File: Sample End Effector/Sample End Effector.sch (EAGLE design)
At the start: 24 parts, among them IC1 LM2936MP-3.0, IC2 LM2936MP-3.0, U2 XBEE-1B3

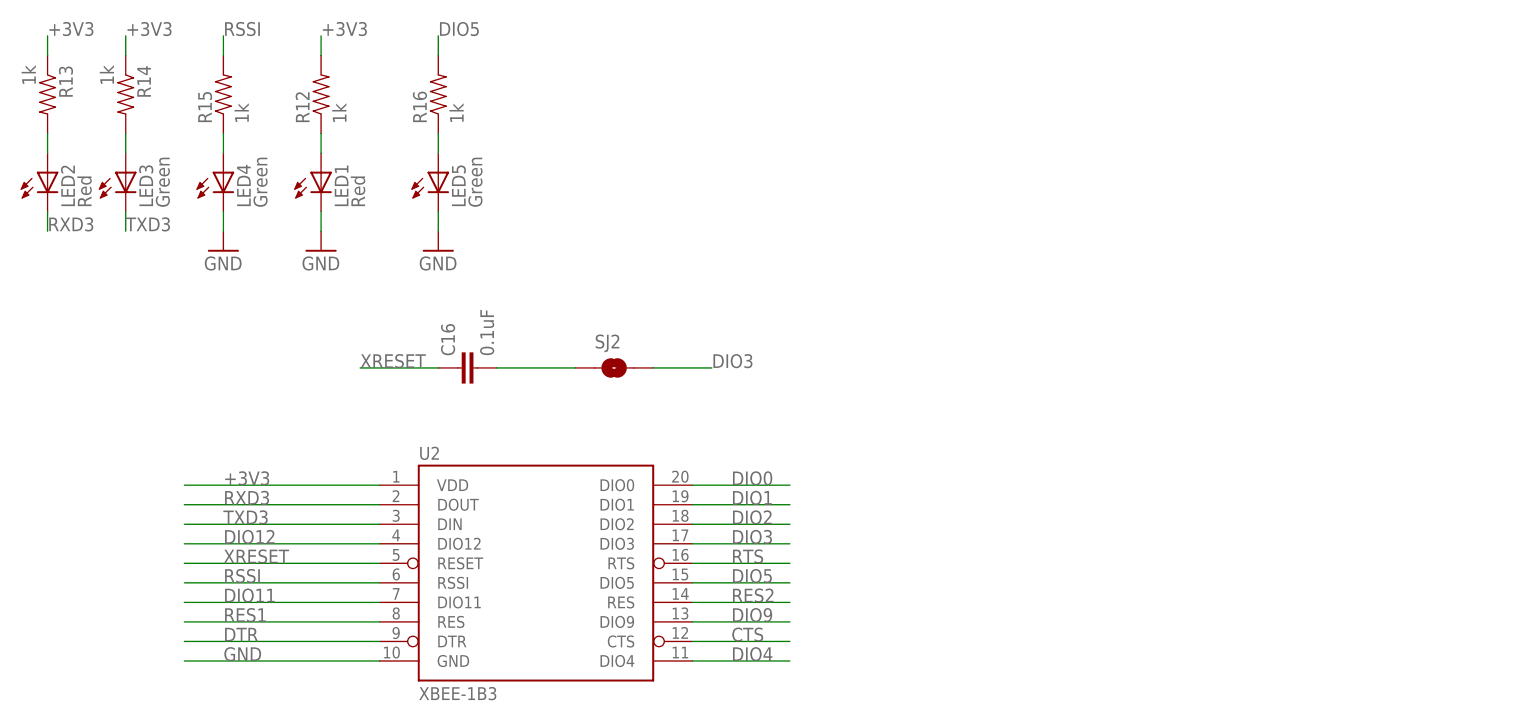
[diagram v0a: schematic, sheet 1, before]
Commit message: Completed the new Sample End Effecter
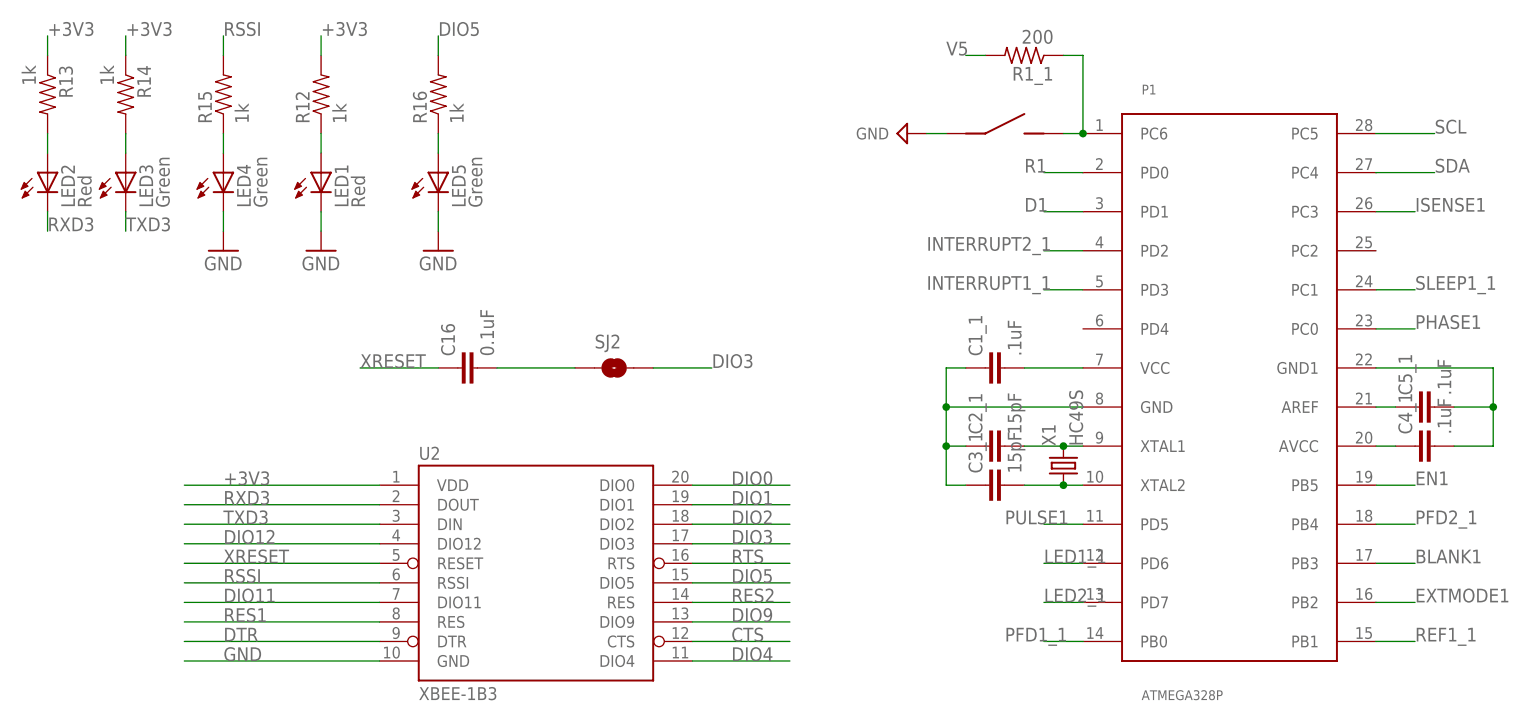
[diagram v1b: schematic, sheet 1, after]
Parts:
- added C1_1, C4_1, C5_1: .1uF, Lib_Passive:C_CAP_0805
- added C2_1, C3_1: 15pF, Lib_Passive:C_CAP_0805
- added P1: ATMEGA328P, PCB0M1:Q_ATMEGA328P
- added R1_1: 200, Lib_Passive:R_RES_0805
- added S1: J_MC32857, PCB0M1:J_MC32857
- added X1: HC49S, PCB0M1:X_HC49SCRYSTAL
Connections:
- new net BLANK1: P1.PB3
- new net D1: P1.PD1
- new net EN1: P1.PB5
- new net EXTMODE1: P1.PB2
- new net INTERRUPT1_1: P1.PD3
- new net INTERRUPT2_1: P1.PD2
- new net ISENSE1: P1.PC3
- new net LED1_1: P1.PD6
- new net LED2_1: P1.PD7
- new net N$1: C3_1.2, P1.XTAL2, X1.1
- new net N$12: C2_1.2, P1.XTAL1, X1.2
- new net N$14: C5_1.1, P1.AREF
- new net N$15: P1.PC6, R1_1.1, S1.2
- new net PFD1_1: P1.PB0
- new net PFD2_1: P1.PB4
- new net PHASE1: P1.PC0
- new net PULSE1: P1.PD5
- new net R1: P1.PD0
- new net REF1_1: P1.PB1
- new net SCL: P1.PC5
- new net SDA: P1.PC4
- new net SLEEP1_1: P1.PC1
- new net V5: C1_1.2, C4_1.1, P1.AVCC, P1.VCC, R1_1.2
- net GND: now also C1_1.1, C2_1.1, C3_1.1, C4_1.2, C5_1.2, P1.GND, P1.GND1, S1.1

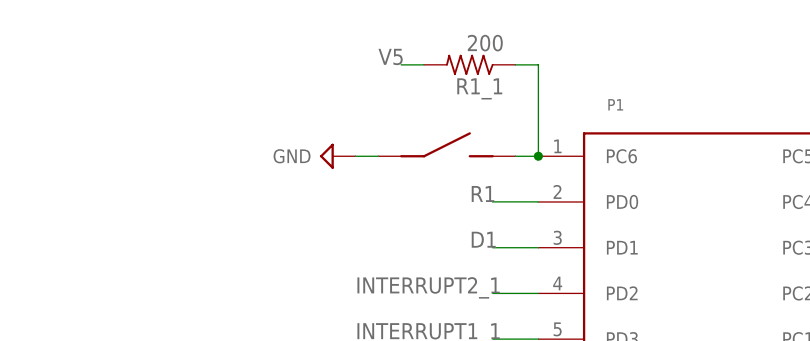
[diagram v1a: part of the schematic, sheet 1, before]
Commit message: Finished sample end effecter and closes #4
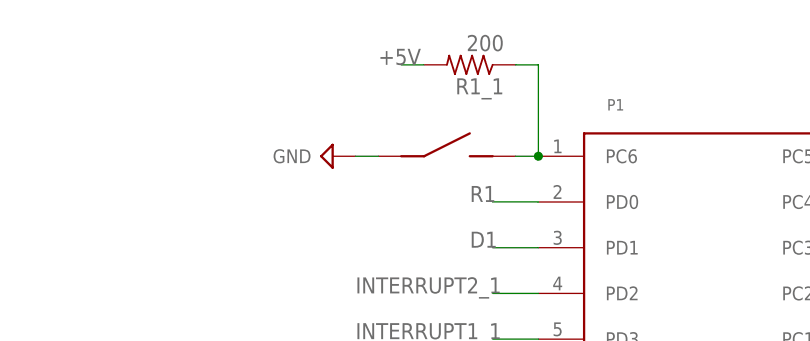
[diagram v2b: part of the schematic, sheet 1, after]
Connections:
- removed net V5: C1_1.2, C4_1.1, P1.AVCC, P1.VCC, R1_1.2
- net +5V: now also C1_1.2, C4_1.1, P1.AVCC, P1.VCC, R1_1.2
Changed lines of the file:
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@@
 </segment>
 </net>
-<net name="V5" class="0">
+<net name="+5V" class="0">
 <segment>
 <pinref part="C1_1" gate="G$1" pin="2"/>
